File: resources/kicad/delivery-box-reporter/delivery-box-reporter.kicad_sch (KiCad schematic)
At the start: 11 parts, among them J1 Solar Panel, Q2 2N3904, U1 ESP8266 D1 Mini, U4 TLV803EB33VDBZR, U5 MCP1702-3302E

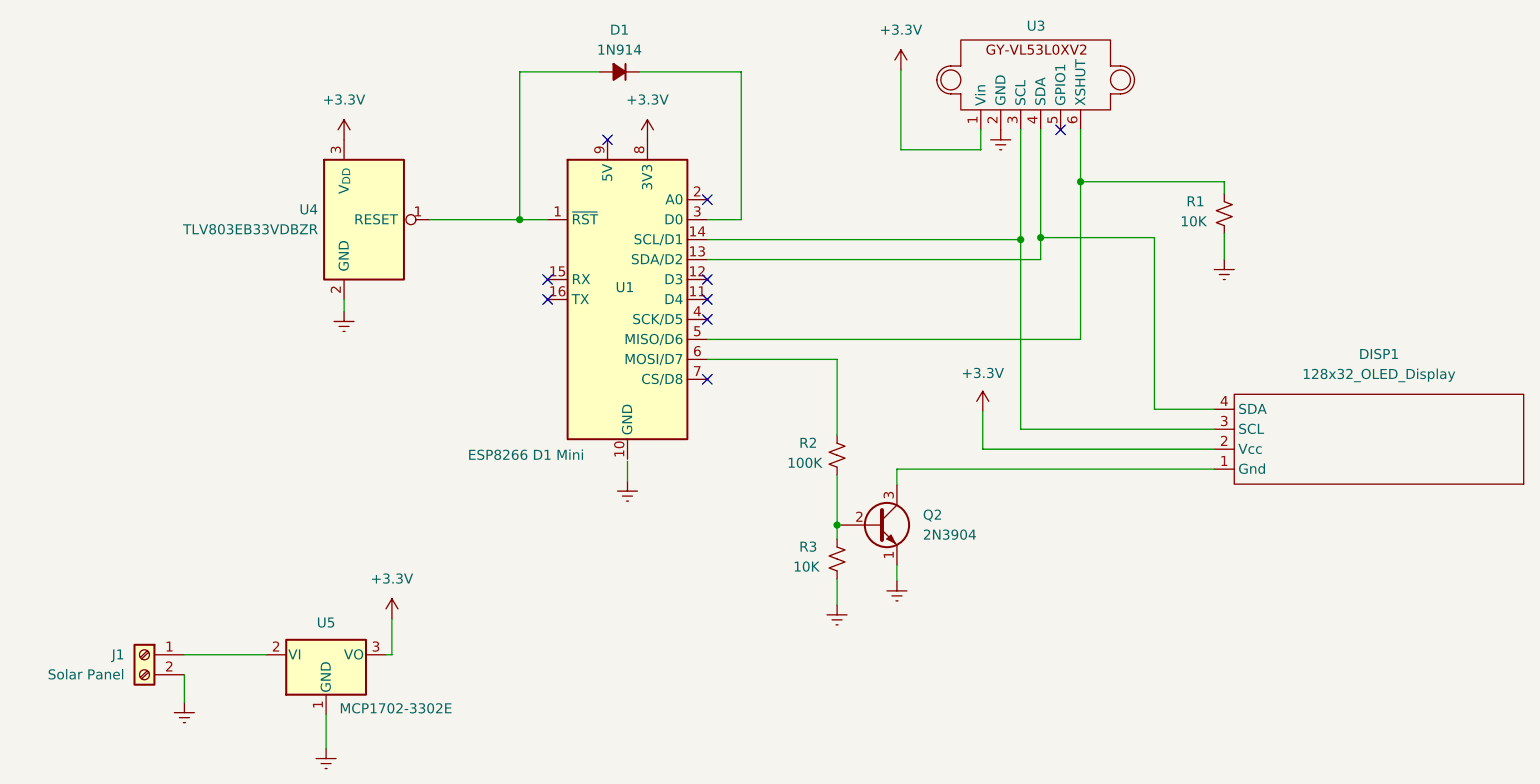
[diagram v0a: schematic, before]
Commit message: Changes to board and minor code changes.
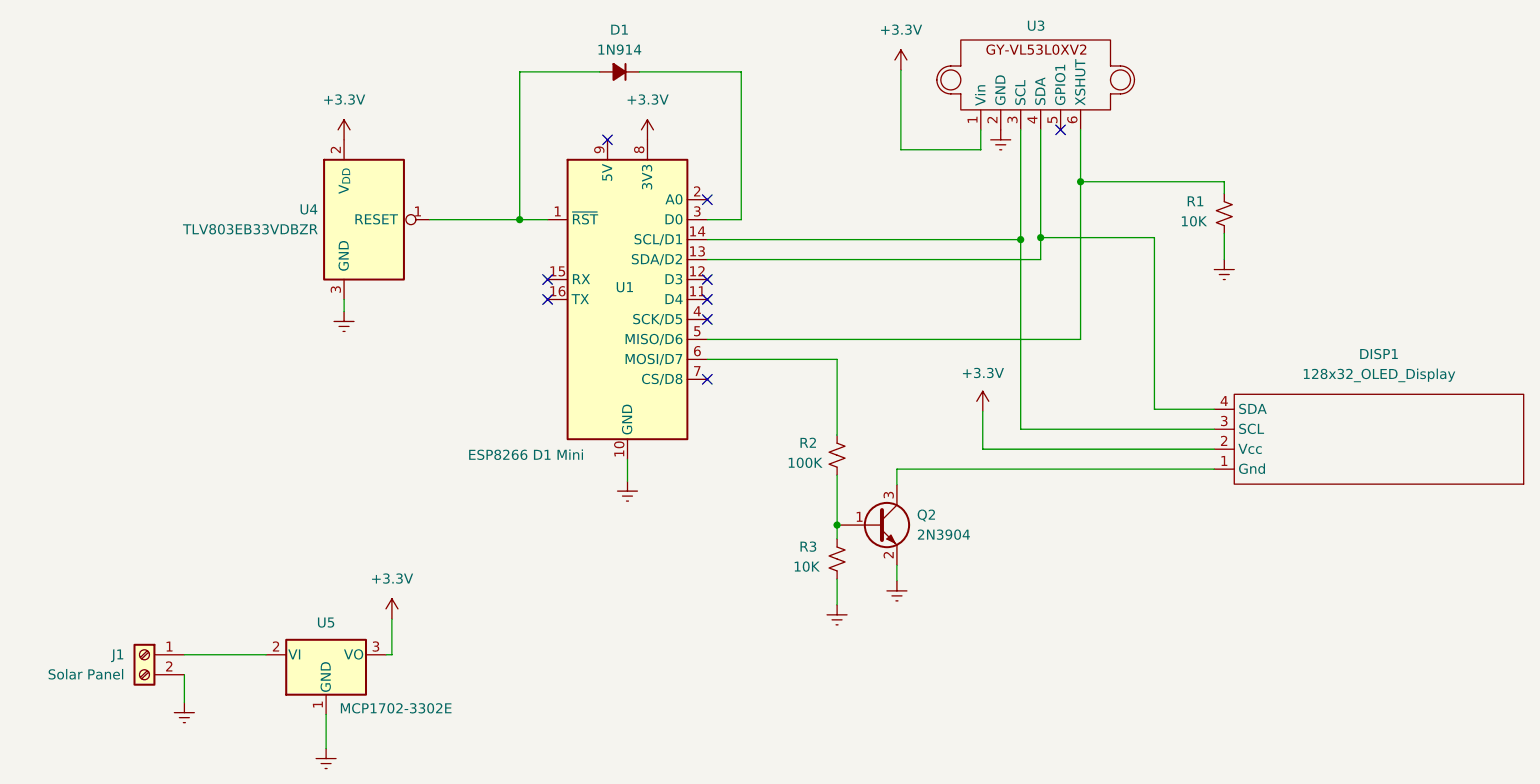
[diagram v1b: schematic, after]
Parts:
- Q2: footprint Package_TO_SOT_SMD:SOT-23 -> Davids_Footprints:MMBT3904-7-F_SOT-23-3; symbol Transistor_BJT:2N3904 -> Davids_Symbols:MMBT3904-7-F_SOT-23
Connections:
- net +3.3V: now also U4.2 (V_{DD}); no longer U4.3 (V_{DD})
- net Earth: now also Q2.2 (E), U1.10 (GND), U4.3 (GND); no longer Q2.1 (E), U4.2 (GND)
- net at R2.1, R3.2: now also Q2.1 (B); no longer Q2.2 (B)
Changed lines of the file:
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@@
 	(wire
 		(pts
-			(xy 124.46 118.618) (xy 124.46 121.158)
+			(xy 124.46 118.364) (xy 124.46 121.158)
 		)
 		(stroke
@@
 		)
 		(property "Datasheet" "http://ww1.microchip.com/downloads/en/DeviceDoc/20001826D.pdf"
-			(at 86.106 143.256 0)
+			(at 84.582 155.194 0)
 			(effects
 				(font
@@
 		)
 		(property "Description" "250mA Low Quiscent Current LDO, 3.3V output, TO-92"
-			(at 86.106 143.256 0)
+			(at 82.804 135.89 0)
 			(effects
 				(font
@@
 	)
 	(symbol
-		(lib_id "Transistor_BJT:2N3904")
+		(lib_id "Davids_Symbols:MMBT3904-7-F_SOT-23")
 		(at 156.21 126.746 0)
 		(unit 1)
@@
 		(fields_autoplaced yes)
 		(property "Reference" "Q2"
-			(at 162.052 125.4759 0)
+			(at 161.29 125.4759 0)
 			(effects
 				(font
@@
 		)
 		(property "Value" "2N3904"
-			(at 162.052 128.0159 0)
+			(at 161.29 128.0159 0)
 			(effects
 				(font
@@
 			)
 		)
-		(property "Footprint" "Package_TO_SOT_SMD:SOT-23"
-			(at 161.29 128.651 0)
+		(property "Footprint" "Davids_Footprints:MMBT3904-7-F_SOT-23-3"
+			(at 140.208 140.716 0)
 			(effects
 				(font
@@
 		)
 		(property "Datasheet" "https://www.onsemi.com/pub/Collateral/2N3903-D.PDF"
-			(at 156.21 126.746 0)
+			(at 132.08 138.176 0)
 			(effects
 				(font
@@
 		)
 		(property "Description" "0.2A Ic, 40V Vce, Small Signal NPN Transistor, TO-92"
-			(at 156.21 126.746 0)
+			(at 155.956 113.03 0)
 			(effects
 				(font
@@
 		)
 		(property "Footprint" "Davids_Footprints:KF350 2 Pin Terminal Block"
-			(at 62.992 143.256 0)
+			(at 64.262 138.938 0)
 			(effects
 				(font
@@
 		)
 		(property "Description" "Generic screw terminal, single row, 01x02, script generated (kicad-library-utils/schlib/autogen/connector/)"
-			(at 62.992 143.256 0)
-			(effects
-				(font
+			(at 64.262 138.938 0)
+			(effects
+				(font

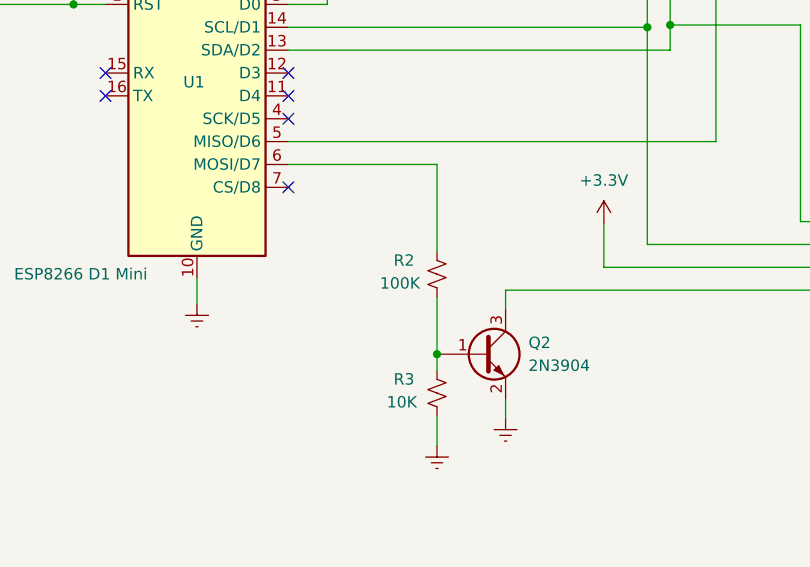
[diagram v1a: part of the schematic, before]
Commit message: Combined overloaded show() functions
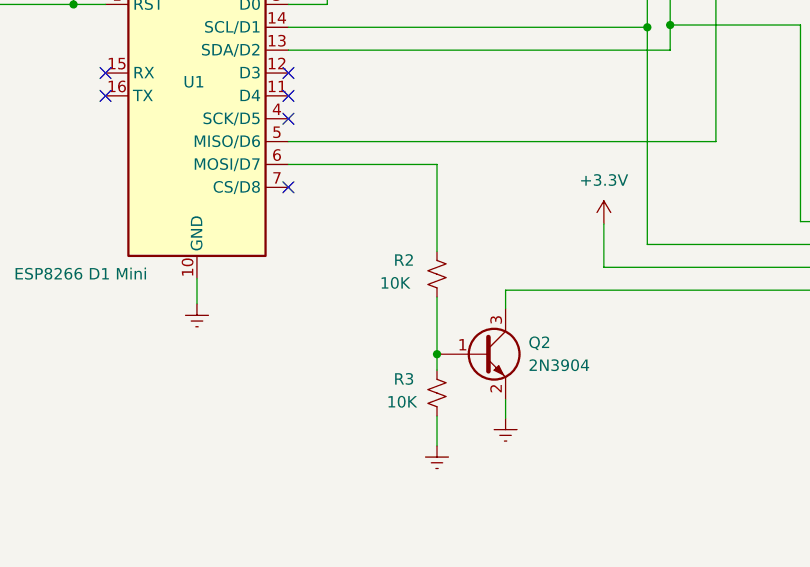
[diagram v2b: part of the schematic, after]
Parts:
- R2: value 100K -> 10K
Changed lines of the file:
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@@
 			)
 		)
-		(property "Value" "100K"
+		(property "Value" "10K"
 			(at 144.78 118.872 0)
 			(effects
